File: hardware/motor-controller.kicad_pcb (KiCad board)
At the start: 2 copper layers, 75 x 50 mm, 56 parts, among them M1 Mounting Hole, M2 Mounting Hole, M3 Mounting Hole, M4 Mounting Hole, P1 VTEST, P101 BATTERY, P102 SWD, P103 EDISON-BULB-E10, P104 FTDI-PLUG, P201 P06-MOTOR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

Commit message: initial
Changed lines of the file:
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@@
-      (net 2 GNDPWR))
-  )
-  (module kicadlib:LGA12S50P4X4_192X192X100 (layer F.Cu)
-    (at 128.361457 107.294165 180)
-    (fp_text reference U102 (at -2.3 0.8 180) (layer F.SilkS)
-      (effects (font (size 0.6 0.6) (thickness 0.1)))
-    )
-    (fp_text value ST-LIS3MDL (at 0 0 180) (layer F.Fab)
-      (effects (font (size 0.6 0.6) (thickness 0.1)))
-    )
-    (fp_circle (center -1.6 -1.6) (end -1.4 -1.6) (layer F.SilkS) (width 0.4))
-    (fp_line (start -2 -2) (end 2 -2) (layer F.CrtYd) (width 0.15))
-    (fp_line (start 2 -2) (end 2 2) (layer F.CrtYd) (width 0.15))
-    (fp_line (start 2 2) (end -2 2) (layer F.CrtYd) (width 0.15))
-    (fp_line (start -2 2) (end -2 -2) (layer F.CrtYd) (width 0.15))
-    (fp_line (start -1 -1) (end 1 -1) (layer F.SilkS) (width 0.15))
-    (fp_line (start 1 -1) (end 1 1) (layer F.SilkS) (width 0.15))
-    (fp_line (start 1 1) (end -1 1) (layer F.SilkS) (width 0.15))
-    (fp_line (start -1 1) (end -1 -1) (layer F.SilkS) (width 0.15))
-    (pad 1 smd rect (at -0.75 -0.75 180) (size 0.25 0.25) (layers F.Cu F.Paste F.Mask)
-      (net 23 /I2CSCL))
-    (pad 2 smd rect (at -0.75 -0.25 180) (size 0.25 0.25) (layers F.Cu F.Paste F.Mask)
-      (net 2 GNDPWR))
-    (pad 3 smd rect (at -0.75 0.25 180) (size 0.25 0.25) (layers F.Cu F.Paste F.Mask)
-      (net 2 GNDPWR))
-    (pad 4 smd rect (at -0.75 0.75 180) (size 0.25 0.25) (layers F.Cu F.Paste F.Mask)
-      (net 3 "Net-(C106-Pad1)"))
-    (pad 5 smd rect (at -0.25 0.75 180) (size 0.25 0.25) (layers F.Cu F.Paste F.Mask)
-      (net 1 +3.3V))
-    (pad 6 smd rect (at 0.25 0.75 180) (size 0.25 0.25) (layers F.Cu F.Paste F.Mask)
-      (net 1 +3.3V))
-    (pad 7 smd rect (at 0.75 0.75 180) (size 0.25 0.25) (layers F.Cu F.Paste F.Mask)
-      (net 61 /COMPASSINT))
-    (pad 8 smd rect (at 0.75 0.25 180) (size 0.25 0.25) (layers F.Cu F.Paste F.Mask)
-      (net 60 /COMPASSDRDY))
-    (pad 9 smd rect (at 0.75 -0.25 180) (size 0.25 0.25) (layers F.Cu F.Paste F.Mask)
-      (net 1 +3.3V))
-    (pad 10 smd rect (at 0.75 -0.75 180) (size 0.25 0.25) (layers F.Cu F.Paste F.Mask)
-      (net 1 +3.3V))
-    (pad 11 smd rect (at 0.25 -0.75 180) (size 0.25 0.25) (layers F.Cu F.Paste F.Mask)
-      (net 22 /I2CSDA))
-    (pad 12 smd rect (at -0.25 -0.75 180) (size 0.25 0.25) (layers F.Cu F.Paste F.Mask)
       (net 2 GNDPWR))
   )
@@
       (net 1 +3.3V))
   )
+  (module kicadlib:LGA12S50P4X4_192X192X100 (layer F.Cu)
+    (at 128.361457 107.294165 180)
+    (fp_text reference U102 (at -2.238543 1.494165 180) (layer F.SilkS)
+      (effects (font (size 0.6 0.6) (thickness 0.1)))
+    )
+    (fp_text value ST-LIS3MDL (at 0 0 180) (layer F.Fab)
+      (effects (font (size 0.6 0.6) (thickness 0.1)))
+    )
+    (fp_line (start 1.2 1.2) (end 0.508 1.2) (layer F.SilkS) (width 0.15))
+    (fp_line (start 1.2 0.508) (end 1.2 1.2) (layer F.SilkS) (width 0.15))
+    (fp_line (start -1.2 -1.2) (end -1.2 -0.508) (layer F.SilkS) (width 0.15))
+    (fp_line (start -0.508 -1.2) (end -1.2 -1.2) (layer F.SilkS) (width 0.15))
+    (fp_circle (center -1.6 -1.6) (end -1.4 -1.6) (layer F.SilkS) (width 0.4))
+    (fp_line (start -2 -2) (end 2 -2) (layer F.CrtYd) (width 0.15))
+    (fp_line (start 2 -2) (end 2 2) (layer F.CrtYd) (width 0.15))
+    (fp_line (start 2 2) (end -2 2) (layer F.CrtYd) (width 0.15))
+    (fp_line (start -2 2) (end -2 -2) (layer F.CrtYd) (width 0.15))
+    (fp_line (start -1 -1) (end 1 -1) (layer F.SilkS) (width 0.15))
+    (fp_line (start 1 -1) (end 1 1) (layer F.SilkS) (width 0.15))
+    (fp_line (start 1 1) (end -1 1) (layer F.SilkS) (width 0.15))
+    (fp_line (start -1 1) (end -1 -1) (layer F.SilkS) (width 0.15))
+    (pad 1 smd rect (at -0.75 -0.75 180) (size 0.25 0.25) (layers F.Cu F.Paste F.Mask)
+      (net 23 /I2CSCL))
+    (pad 2 smd rect (at -0.75 -0.25 180) (size 0.25 0.25) (layers F.Cu F.Paste F.Mask)
+      (net 2 GNDPWR))
+    (pad 3 smd rect (at -0.75 0.25 180) (size 0.25 0.25) (layers F.Cu F.Paste F.Mask)
+      (net 2 GNDPWR))
+    (pad 4 smd rect (at -0.75 0.75 180) (size 0.25 0.25) (layers F.Cu F.Paste F.Mask)
+      (net 3 "Net-(C106-Pad1)"))
+    (pad 5 smd rect (at -0.25 0.75 180) (size 0.25 0.25) (layers F.Cu F.Paste F.Mask)
+      (net 1 +3.3V))
+    (pad 6 smd rect (at 0.25 0.75 180) (size 0.25 0.25) (layers F.Cu F.Paste F.Mask)
+      (net 1 +3.3V))
+    (pad 7 smd rect (at 0.75 0.75 180) (size 0.25 0.25) (layers F.Cu F.Paste F.Mask)
+      (net 61 /COMPASSINT))
+    (pad 8 smd rect (at 0.75 0.25 180) (size 0.25 0.25) (layers F.Cu F.Paste F.Mask)
+      (net 60 /COMPASSDRDY))
+    (pad 9 smd rect (at 0.75 -0.25 180) (size 0.25 0.25) (layers F.Cu F.Paste F.Mask)
+      (net 1 +3.3V))
+    (pad 10 smd rect (at 0.75 -0.75 180) (size 0.25 0.25) (layers F.Cu F.Paste F.Mask)
+      (net 1 +3.3V))
+    (pad 11 smd rect (at 0.25 -0.75 180) (size 0.25 0.25) (layers F.Cu F.Paste F.Mask)
+      (net 22 /I2CSDA))
+    (pad 12 smd rect (at -0.25 -0.75 180) (size 0.25 0.25) (layers F.Cu F.Paste F.Mask)
+      (net 2 GNDPWR))
+  )
   (gr_line (start 113 150) (end 113 100) (angle 90) (layer Edge.Cuts) (width 0.1))

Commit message: layout
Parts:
- added D1: STATUS, kicadlib:LEDC3216X100N, F.Cu at (147.4, 143.0)
- added R1: 100R, kicadlib:RESC2012X100N, F.Cu at (145.0, 143.6)
- added R2: 1K, kicadlib:RESC2012X100N, F.Cu at (149.2, 132.8)
- added R3: 1K, kicadlib:RESC2012X100N, F.Cu at (146.8, 132.8)
- added R4: 1K, kicadlib:RESC2012X100N, F.Cu at (148.2, 120.5)
- added R5: 1K, kicadlib:RESC2012X100N, F.Cu at (148.2, 126.6)
- added S1: RESET, kicadlib:CKCOMP-PTS525SM10SMTR, F.Cu at (128.6, 127.0)
- U101: value STM32F030K6T6 -> STM32L051K8T6
- moved C103 19.2 mm to (147.0, 137.4), turned to 270 degrees
- moved C101 14.8 mm to (143.2, 131.6), turned to 0 degrees
- moved C102 12.7 mm to (131.4, 142.4)
- moved U101 3.32 mm to (138.0, 137.4), turned to 225 degrees
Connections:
- U101 pad 14: /drivers/MOTORLCHA -> /NIRQ
- U101 pad 15: /drivers/MOTORLCHB -> /drivers/MOTOREN
- U101 pad 18: /drivers/MOTORLPWM -> Net-(U101-Pad18)
- U101 pad 19: /drivers/MOTORLDIR -> /USARTTX
- U101 pad 2: Net-(U101-Pad2) -> /drivers/MOTORRDIR
- U101 pad 20: /drivers/MOTORRPWM -> /USARTRX
- U101 pad 21: /drivers/MOTORRDIR -> /drivers/MOTORRCHB
- U101 pad 22: /drivers/MOTOREN -> /drivers/MOTORRCHA
- U101 pad 25: /COMPASSDRDY -> /STATUS
- U101 pad 26: /COMPASSINT -> Net-(U101-Pad26)
- U101 pad 27: /drivers/MOTORRCHA -> /COMPASSINT
- U101 pad 28: /drivers/MOTORRCHB -> /COMPASSDRDY
- U101 pad 3: Net-(U101-Pad3) -> /drivers/MOTORLDIR
- U101 pad 6: Net-(U101-Pad6) -> /drivers/MOTORLPWM
- U101 pad 7: /NIRQ -> /drivers/MOTORRPWM
- U101 pad 8: /USARTTX -> /drivers/MOTORLCHA
- U101 pad 9: /USARTRX -> /drivers/MOTORLCHB
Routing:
- net +5V: track 112.9 -> 147.6 mm, vias 2 -> 7
- net /drivers/MOTORRCHB: track 11.5 -> 28.8 mm
- net /drivers/MOTORRCHA: track 13.7 -> 30.7 mm
- net /drivers/MOTORLPWM: track 46.9 -> 30.1 mm, vias 4 -> 0
- net /COMPASSINT: track 38.8 -> 54.2 mm, vias 2 -> 4
- net /COMPASSDRDY: track 37.5 -> 52.3 mm, vias 2 -> 4
- net /I2CSDA: track 34.6 -> 48.0 mm, vias 2 -> 4
- net /drivers/MOTOREN: track 57.6 -> 68.8 mm, vias 5 -> 9
- net /I2CSCL: track 33.6 -> 44.3 mm, vias 2 -> 5
- net +3.3V: track 271.7 -> 280.0 mm, vias 6 -> 8
- net /STATUS: track 0.00 -> 6.92 mm
- net /drivers/MOTORRPWM: track 45.6 -> 39.3 mm, vias 6 -> 4
- net /drivers/MOTORLCHA: track 13.6 -> 7.83 mm
- net /drivers/MOTORROUTCHB: track 67.4 -> 72.6 mm, vias 2 -> 3
- net /drivers/MOTORROUTCHA: track 66.6 -> 71.7 mm
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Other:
- board text added: "2016-01-03"
- board text added: "LEFT"
- board text added: "RESET"
- board text added: "RIGHT"
- board text added: "STATUS"
- board text removed: "2015-11-12"

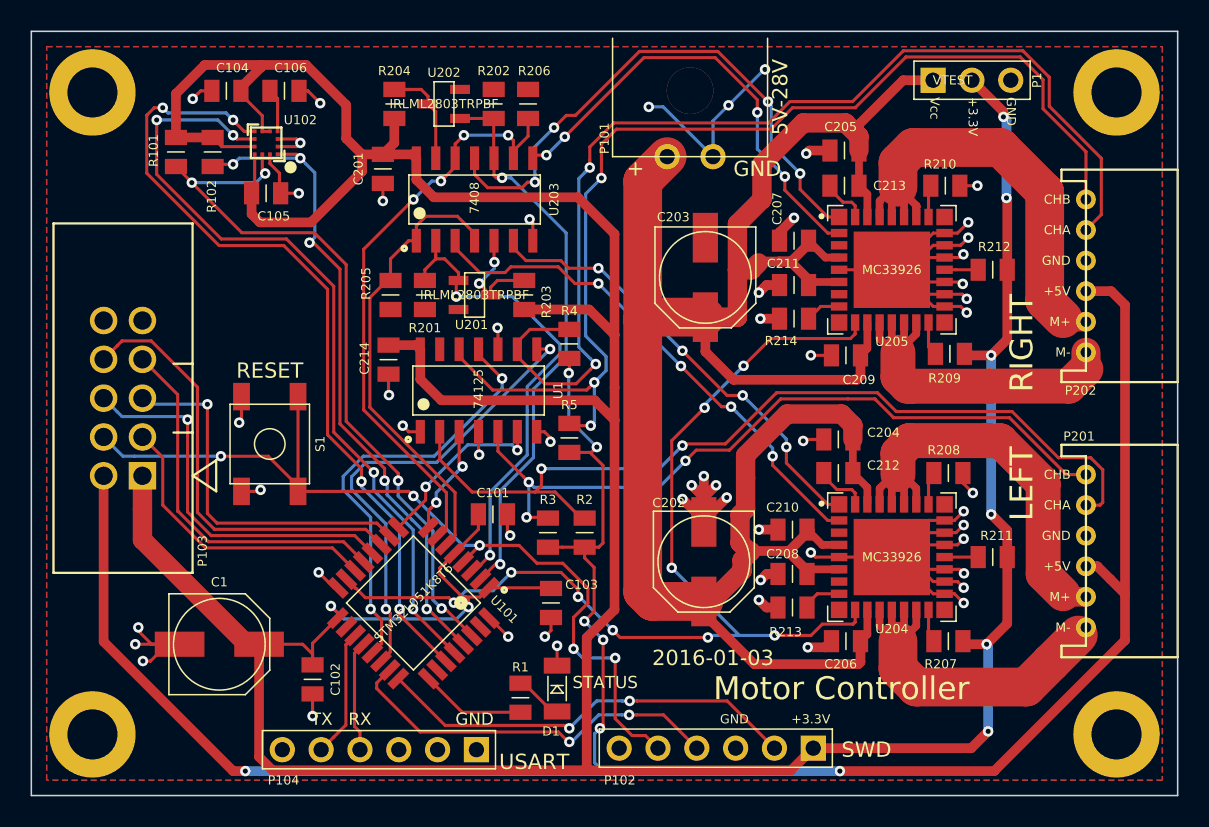
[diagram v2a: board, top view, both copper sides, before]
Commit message: compass x/y
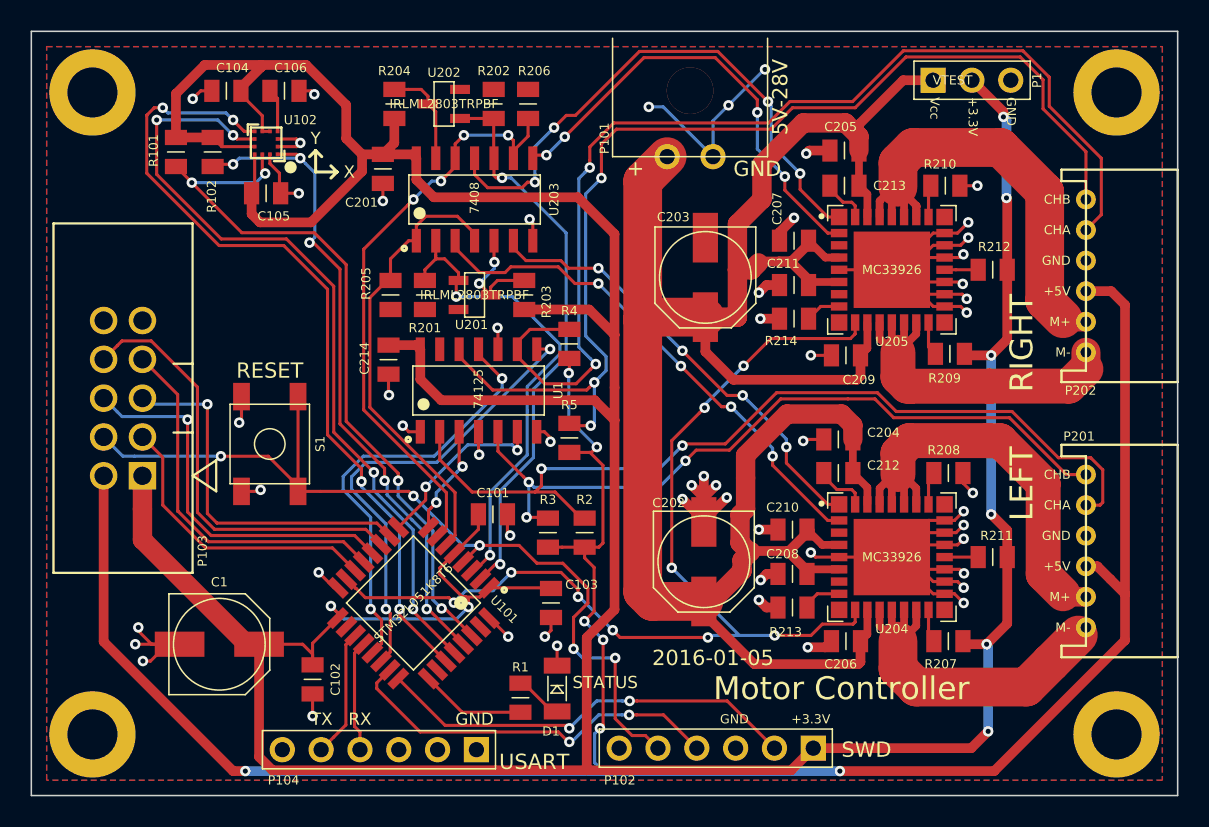
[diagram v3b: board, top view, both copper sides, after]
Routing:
- net GNDPWR: track 158.3 -> 157.7 mm
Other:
- board text added: "2016-01-05"
- board text added: "X"
- board text added: "Y"
- board text removed: "2016-01-03"
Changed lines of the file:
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@@
     (links 203)
     (no_connects 0)
-    (area 112.949999 99.949999 188.050001 150.050001)
+    (area 112.949999 98.475999 193.729001 150.407)
     (thickness 1.6)
-    (drawings 36)
+    (drawings 44)
     (tracks 1114)
     (zones 0)
@@
   (module kicadlib:CAPC2012X100N (layer F.Cu)
     (at 136 109 270)
-    (fp_text reference C201 (at 0 1.6 450) (layer F.SilkS)
+    (fp_text reference C201 (at 2.2 1.4 540) (layer F.SilkS)
       (effects (font (size 0.6 0.6) (thickness 0.1)))
     )
@@
       (net 9 /NRST))
   )
+  (gr_line (start 131.6 107.8) (end 131.6 109.2) (layer F.SilkS) (width 0.2))
+  (gr_text Y (at 131.6 107) (layer F.SilkS)
+    (effects (font (size 0.8 0.8) (thickness 0.2)))
+  )
+  (gr_line (start 131.6 107.8) (end 131.2 108.2) (layer F.SilkS) (width 0.2))
+  (gr_line (start 131.6 107.8) (end 132 108.2) (layer F.SilkS) (width 0.2))
+  (gr_text X (at 133.8 109.2) (layer F.SilkS)
+    (effects (font (size 0.8 0.8) (thickness 0.2)))
+  )
+  (gr_line (start 133 109.2) (end 132.6 108.8) (layer F.SilkS) (width 0.2))
+  (gr_line (start 133 109.2) (end 132.6 109.6) (layer F.SilkS) (width 0.2))
+  (gr_line (start 131.6 109.2) (end 133 109.2) (layer F.SilkS) (width 0.2))
   (gr_text STATUS (at 148.4 142.6) (layer F.SilkS)
     (effects (font (size 0.8 0.8) (thickness 0.15)) (justify left))
@@
   (gr_line (start 188 100) (end 188 150) (angle 90) (layer Edge.Cuts) (width 0.1))
   (gr_line (start 113 100) (end 188 100) (angle 90) (layer Edge.Cuts) (width 0.1))
-  (gr_text 2016-01-03 (at 157.6 141) (layer F.SilkS)
-    (effects (font (size 1 1) (thickness 0.1)))
+  (gr_text 2016-01-05 (at 157.6 141) (layer F.SilkS)
+    (effects (font (size 1 1) (thickness 0.15)))
   )
   (gr_text "Motor Controller" (at 165.8 143) (layer B.SilkS)
@@
   (segment (start 120.27 133.27) (end 120.27 131.25) (width 1.27) (layer F.Cu) (net 1))
   (segment (start 120.27 131.25) (end 120.27 129.08) (width 1.27) (layer F.Cu) (net 1))
+  (segment (start 131.291803 103.894165) (end 131.516556 104.118918) (width 0.2032) (layer F.Cu) (net 2))
+  (segment (start 130.511457 103.894165) (end 131.291803 103.894165) (width 0.2032) (layer F.Cu) (net 2))
+  (via (at 131.516556 104.118918) (size 0.6858) (drill 0.3302) (layers F.Cu B.Cu) (net 2))
   (segment (start 142.949747 138.389949) (end 142.989949 138.389949) (width 0.2032) (layer F.Cu) (net 2))
   (segment (start 142.989949 138.389949) (end 144.2 139.6) (width 0.2032) (layer F.Cu) (net 2))
@@
   (segment (start 130.344165 107.044165) (end 130.6 107.3) (width 0.2032) (layer F.Cu) (net 2))
   (via (at 130.6 107.3) (size 0.6858) (drill 0.3302) (layers F.Cu B.Cu) (net 2))
-  (segment (start 130.511457 103.894165) (end 131.094165 103.894165) (width 0.2032) (layer F.Cu) (net 2))
-  (segment (start 131.094165 103.894165) (end 131.9 104.7) (width 0.2032) (layer F.Cu) (net 2))
-  (via (at 131.9 104.7) (size 0.6858) (drill 0.3302) (layers F.Cu B.Cu) (net 2))
   (segment (start 136 109.95) (end 136 111.1) (width 0.2032) (layer F.Cu) (net 2))
   (via (at 136 111.1) (size 0.6858) (drill 0.3302) (layers F.Cu B.Cu) (net 2))
